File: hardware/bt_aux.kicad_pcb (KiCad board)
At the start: 2 copper layers, 51.8 x 29 mm, 18 parts, among them J1 esp32_1, J2 esp32_2, J3 audio_out, U1 PCM5102A

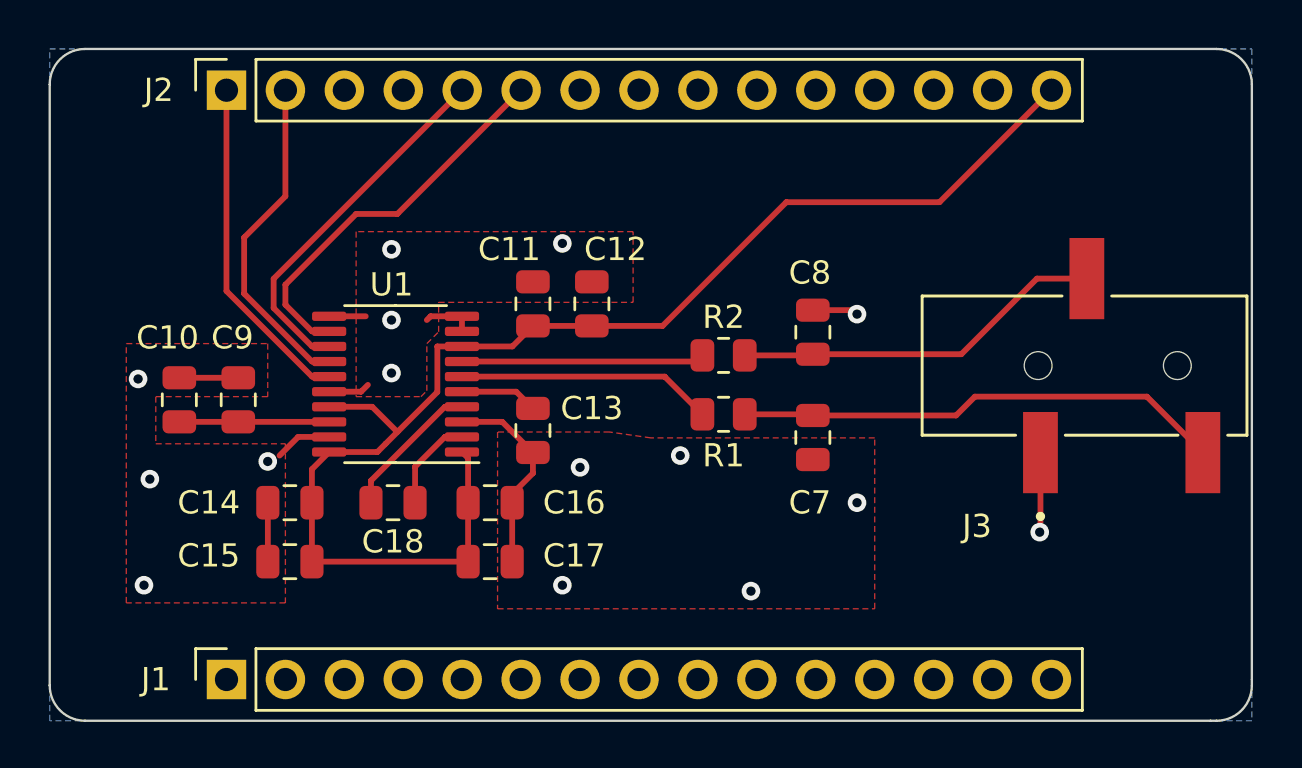
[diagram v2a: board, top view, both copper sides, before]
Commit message: fix oreintation of jack
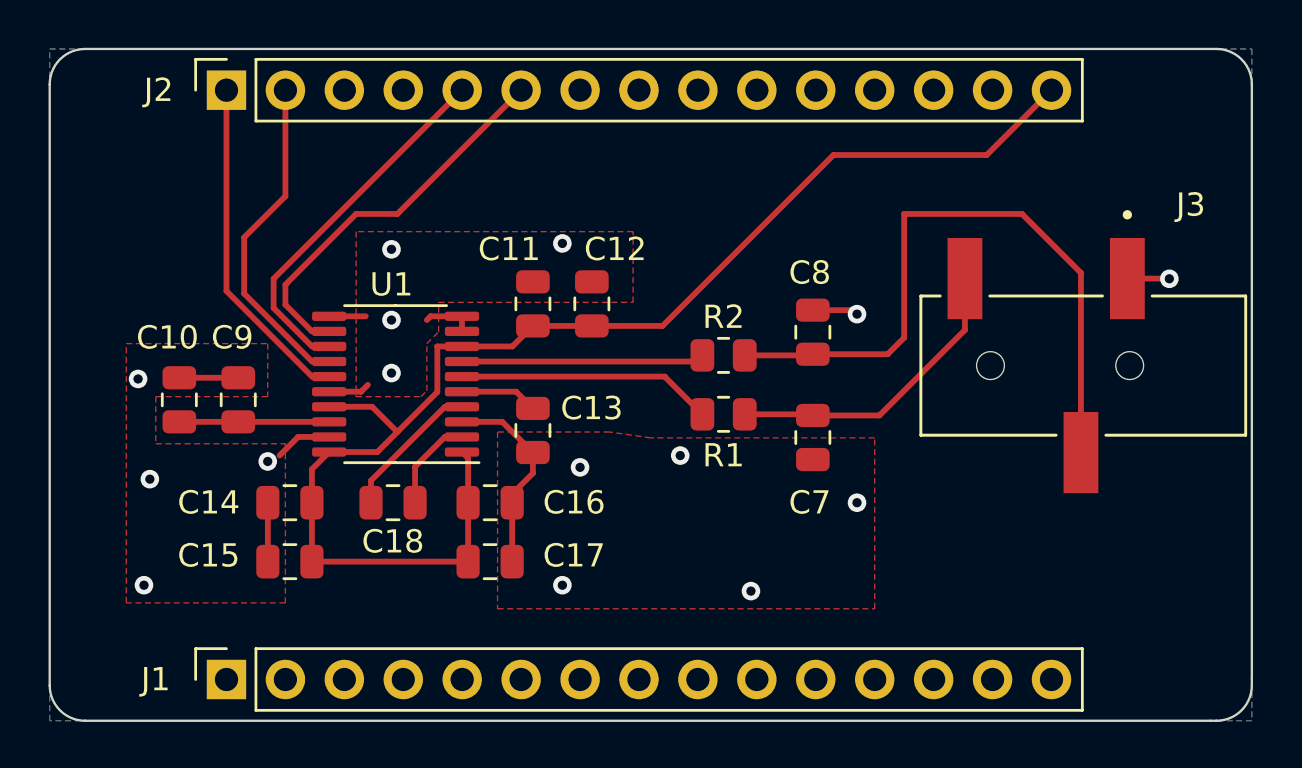
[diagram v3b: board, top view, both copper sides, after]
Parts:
- moved J3 2.05 mm to (163.7, 103.3), turned to 180 degrees
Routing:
- net /right: track 16.1 -> 28.9 mm
- net /left: track 21.1 -> 13.3 mm
- net GND: track 27.5 -> 25.6 mm
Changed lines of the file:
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@@
   )
   (footprint "audio-jack:BOOMELE_PJ-320B" (layer "F.Cu")
-    (at 165.746 103.31)
+    (at 163.692 103.31 180)
     (property "Link" "https://jlcpcb.com/partdetail/boomele_boom_Precision_elec-C18594/C18594")
     (property "Sheetfile" "bt_aux.kicad_sch")
@@
     (fp_circle (center -2.9 6.5) (end -2.8 6.5)
       (stroke (width 0.2) (type solid)) (fill none) (layer "F.Fab"))
-    (pad "" np_thru_hole circle (at -3 0) (size 1.2 1.2) (drill 1.2) (layers "*.Cu" "*.Mask"))
-    (pad "" np_thru_hole circle (at 3 0) (size 1.2 1.2) (drill 1.2) (layers "*.Cu" "*.Mask"))
-    (pad "R" smd rect (at -0.9 -3.75) (size 1.5 3.5) (layers "F.Cu" "F.Paste" "F.Mask")
+    (pad "" np_thru_hole circle (at -3 0 180) (size 1.2 1.2) (drill 1.2) (layers "*.Cu" "*.Mask"))
+    (pad "" np_thru_hole circle (at 3 0 180) (size 1.2 1.2) (drill 1.2) (layers "*.Cu" "*.Mask"))
+    (pad "R" smd rect (at -0.9 -3.75 180) (size 1.5 3.5) (layers "F.Cu" "F.Paste" "F.Mask")
       (net 3 "/right") (pintype "passive") (solder_mask_margin 0.102))
-    (pad "S" smd rect (at -2.9 3.75) (size 1.5 3.5) (layers "F.Cu" "F.Paste" "F.Mask")
+    (pad "S" smd rect (at -2.9 3.75 180) (size 1.5 3.5) (layers "F.Cu" "F.Paste" "F.Mask")
       (net 2 "GND") (pintype "passive") (solder_mask_margin 0.102))
-    (pad "T" smd rect (at 4.1 3.75) (size 1.5 3.5) (layers "F.Cu" "F.Paste" "F.Mask")
+    (pad "T" smd rect (at 4.1 3.75 180) (size 1.5 3.5) (layers "F.Cu" "F.Paste" "F.Mask")
       (net 1 "/left") (pintype "passive") (solder_mask_margin 0.102))
+    (model "/home/bradley/Downloads/User Library-PJ-320B.STEP"
+      (offset (xyz -0.9 0 0))
+      (scale (xyz 1 1 1))
+      (rotate (xyz 0 0 0))
+    )
   )
   (footprint "Resistor_SMD:R_0805_2012Metric" (layer "F.Cu")
@@
     (stroke (width 0.1) (type default)) (layer "Edge.Cuts"))
   (segment (start 152.985 105.41) (end 153.035 105.46) (width 0.25) (layer "F.Cu") (net 1))
-  (segment (start 167.434 104.648) (end 169.846 107.06) (width 0.25) (layer "F.Cu") (net 1))
   (segment (start 150.1 105.41) (end 152.985 105.41) (width 0.25) (layer "F.Cu") (net 1))
-  (segment (start 160.02 104.648) (end 167.434 104.648) (width 0.25) (layer "F.Cu") (net 1))
-  (segment (start 159.208 105.46) (end 160.02 104.648) (width 0.25) (layer "F.Cu") (net 1))
-  (segment (start 153.035 105.46) (end 159.208 105.46) (width 0.25) (layer "F.Cu") (net 1))
+  (segment (start 159.592 101.774) (end 155.906 105.46) (width 0.25) (layer "F.Cu") (net 1))
+  (segment (start 159.592 99.56) (end 159.592 101.774) (width 0.25) (layer "F.Cu") (net 1))
+  (segment (start 155.906 105.46) (end 153.035 105.46) (width 0.25) (layer "F.Cu") (net 1))
   (segment (start 139.649 105.735) (end 137.9125 105.735) (width 0.25) (layer "F.Cu") (net 2))
-  (segment (start 162.846 110.458) (end 162.814 110.49) (width 0.25) (layer "F.Cu") (net 2))
   (segment (start 140.076 108.844) (end 140.97 107.95) (width 0.25) (layer "F.Cu") (net 2))
   (segment (start 128.27 103.835) (end 125.73 103.835) (width 0.25) (layer "F.Cu") (net 2))
   (segment (start 153.035 100.92) (end 154.768 100.92) (width 0.25) (layer "F.Cu") (net 2))
-  (segment (start 162.846 107.06) (end 162.846 110.458) (width 0.25) (layer "F.Cu") (net 2))
   (segment (start 137.9125 101.185) (end 137.9125 101.835) (width 0.25) (layer "F.Cu") (net 2))
   (segment (start 140.076 109.22) (end 140.076 108.844) (width 0.25) (layer "F.Cu") (net 2))
+  (segment (start 168.394 99.56) (end 168.402 99.568) (width 0.25) (layer "F.Cu") (net 2))
   (segment (start 137.9125 101.185) (end 136.559 101.185) (width 0.25) (layer "F.Cu") (net 2))
-  (segment (start 163.01 110.294) (end 162.814 110.49) (width 0.25) (layer "F.Cu") (net 2))
   (segment (start 140.97 107.95) (end 140.97 107.056) (width 0.25) (layer "F.Cu") (net 2))
   (segment (start 132.1875 101.185) (end 133.765 101.185) (width 0.25) (layer "F.Cu") (net 2))
@@
   (segment (start 132.1875 106.385) (end 130.851 106.385) (width 0.25) (layer "F.Cu") (net 2))
   (segment (start 140.97 107.056) (end 139.649 105.735) (width 0.25) (layer "F.Cu") (net 2))
+  (segment (start 166.592 99.56) (end 168.394 99.56) (width 0.25) (layer "F.Cu") (net 2))
   (via (at 142.24 112.776) (size 0.8) (drill 0.4) (layers "F.Cu" "B.Cu") (free) (net 2))
   (via (at 124.206 112.776) (size 0.8) (drill 0.4) (layers "F.Cu" "B.Cu") (free) (net 2))
@@
   (via (at 142.24 98.044) (size 0.8) (drill 0.4) (layers "F.Cu" "B.Cu") (free) (net 2))
   (via (at 147.32 107.188) (size 0.8) (drill 0.4) (layers "F.Cu" "B.Cu") (free) (net 2))
+  (via (at 168.402 99.568) (size 0.8) (drill 0.4) (layers "F.Cu" "B.Cu") (net 2))
   (via (at 154.94 109.22) (size 0.8) (drill 0.4) (layers "F.Cu" "B.Cu") (free) (net 2))
   (via (at 150.368 113.03) (size 0.8) (drill 0.4) (layers "F.Cu" "B.Cu") (free) (net 2))
@@
   (via (at 134.874 98.298) (size 0.8) (drill 0.4) (layers "F.Cu" "B.Cu") (free) (net 2))
   (via (at 124.46 108.204) (size 0.8) (drill 0.4) (layers "F.Cu" "B.Cu") (free) (net 2))
-  (via (at 162.814 110.49) (size 0.8) (drill 0.4) (layers "F.Cu" "B.Cu") (net 2))
   (via (at 143.002 107.696) (size 0.8) (drill 0.4) (layers "F.Cu" "B.Cu") (free) (net 2))
   (via (at 134.874 103.632) (size 0.8) (drill 0.4) (layers "F.Cu" "B.Cu") (free) (net 2))
   (via (at 154.94 101.092) (size 0.8) (drill 0.4) (layers "F.Cu" "B.Cu") (net 2))
   (via (at 134.874 101.346) (size 0.8) (drill 0.4) (layers "F.Cu" "B.Cu") (free) (net 2))
-  (segment (start 162.695 99.56) (end 164.846 99.56) (width 0.25) (layer "F.Cu") (net 3))
-  (segment (start 153.035 102.82) (end 159.435 102.82) (width 0.25) (layer "F.Cu") (net 3))
+  (segment (start 156.972 102.108) (end 156.26 102.82) (width 0.25) (layer "F.Cu") (net 3))
+  (segment (start 164.592 99.314) (end 162.052 96.774) (width 0.25) (layer "F.Cu") (net 3))
+  (segment (start 156.26 102.82) (end 153.035 102.82) (width 0.25) (layer "F.Cu") (net 3))
+  (segment (start 162.052 96.774) (end 156.972 96.774) (width 0.25) (layer "F.Cu") (net 3))
   (segment (start 150.1 102.87) (end 152.985 102.87) (width 0.25) (layer "F.Cu") (net 3))
+  (segment (start 156.972 96.774) (end 156.972 102.108) (width 0.25) (layer "F.Cu") (net 3))
   (segment (start 152.985 102.87) (end 153.035 102.82) (width 0.25) (layer "F.Cu") (net 3))
-  (segment (start 159.435 102.82) (end 162.695 99.56) (width 0.25) (layer "F.Cu") (net 3))
+  (segment (start 164.592 107.06) (end 164.592 99.314) (width 0.25) (layer "F.Cu") (net 3))
   (segment (start 128.265 105.405) (end 128.27 105.41) (width 0.25) (layer "F.Cu") (net 4))
   (segment (start 128.27 105.735) (end 125.73 105.735) (width 0.25) (layer "F.Cu") (net 4))
@@
   (segment (start 134.041 105.085) (end 135.128 106.172) (width 0.25) (layer "F.Cu") (net 5))
   (segment (start 134.265 107.035) (end 132.1875 107.035) (width 0.25) (layer "F.Cu") (net 5))
-  (segment (start 158.496 96.266) (end 151.892 96.266) (width 0.25) (layer "F.Cu") (net 5))
+  (segment (start 146.558 101.6) (end 143.51 101.6) (width 0.25) (layer "F.Cu") (net 5))
   (segment (start 131.445 107.7775) (end 132.1875 107.035) (width 0.25) (layer "F.Cu") (net 5))
   (segment (start 137.9125 102.485) (end 136.85 102.485) (width 0.25) (layer "F.Cu") (net 5))
   (segment (start 136.85 104.45) (end 134.62 106.68) (width 0.25) (layer "F.Cu") (net 5))
+  (segment (start 160.528 94.234) (end 153.924 94.234) (width 0.25) (layer "F.Cu") (net 5))
   (segment (start 134.62 106.68) (end 134.265 107.035) (width 0.25) (layer "F.Cu") (net 5))
   (segment (start 131.445 111.76) (end 138.176 111.76) (width 0.25) (layer "F.Cu") (net 5))
   (segment (start 131.445 109.22) (end 131.445 107.7775) (width 0.25) (layer "F.Cu") (net 5))
-  (segment (start 151.892 96.266) (end 146.558 101.6) (width 0.25) (layer "F.Cu") (net 5))
   (segment (start 131.445 111.76) (end 131.445 109.22) (width 0.25) (layer "F.Cu") (net 5))
   (segment (start 136.85 102.485) (end 136.85 104.45) (width 0.25) (layer "F.Cu") (net 5))
   (segment (start 138.176 107.2985) (end 137.9125 107.035) (width 0.25) (layer "F.Cu") (net 5))
-  (segment (start 146.558 101.6) (end 143.51 101.6) (width 0.25) (layer "F.Cu") (net 5))
+  (segment (start 163.322 91.44) (end 160.528 94.234) (width 0.25) (layer "F.Cu") (net 5))
   (segment (start 140.97 101.6) (end 140.085 102.485) (width 0.25) (layer "F.Cu") (net 5))
-  (segment (start 163.322 91.44) (end 158.496 96.266) (width 0.25) (layer "F.Cu") (net 5))
+  (segment (start 153.924 94.234) (end 146.558 101.6) (width 0.25) (layer "F.Cu") (net 5))
   (segment (start 140.249 104.435) (end 137.9125 104.435) (width 0.25) (layer "F.Cu") (net 6))
   (segment (start 140.97 105.156) (end 140.249 104.435) (width 0.25) (layer "F.Cu") (net 6))

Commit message: modify bom, generate fab files, submit order
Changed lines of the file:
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@@
       (outputformat 1)
       (mirror false)
-      (drillshape 1)
+      (drillshape 0)
       (scaleselection 1)
-      (outputdirectory "")
+      (outputdirectory "fab/")
     )
   )
@@
     (fp_line (start 1 0.625) (end -1 0.625)
       (stroke (width 0.1) (type solid)) (layer "F.Fab"))
-    (pad "1" smd roundrect (at -0.9125 0) (size 1.025 1.4) (layers "F.Cu" "F.Paste" "F.Mask") (roundrect_rratio 0.243902)
+    (pad "1" smd roundrect (at -0.9125 0) (size 1.025 1.4) (layers "F.Cu" "F.Paste" "F.Mask") (roundrect_rratio 0.243902439)
       (net 32 "Net-(U1-OUTL)") (pintype "passive"))
-    (pad "2" smd roundrect (at 0.9125 0) (size 1.025 1.4) (layers "F.Cu" "F.Paste" "F.Mask") (roundrect_rratio 0.243902)
+    (pad "2" smd roundrect (at 0.9125 0) (size 1.025 1.4) (layers "F.Cu" "F.Paste" "F.Mask") (roundrect_rratio 0.243902439)
       (net 1 "/left") (pintype "passive"))
     (model "${KICAD6_3DMODEL_DIR}/Resistor_SMD.3dshapes/R_0805_2012Metric.wrl"
@@
     (fp_line (start 1 0.625) (end -1 0.625)
       (stroke (width 0.1) (type solid)) (layer "F.Fab"))
-    (pad "1" smd roundrect (at -0.9125 0) (size 1.025 1.4) (layers "F.Cu" "F.Paste" "F.Mask") (roundrect_rratio 0.243902)
+    (pad "1" smd roundrect (at -0.9125 0) (size 1.025 1.4) (layers "F.Cu" "F.Paste" "F.Mask") (roundrect_rratio 0.243902439)
       (net 33 "Net-(U1-OUTR)") (pintype "passive"))
-    (pad "2" smd roundrect (at 0.9125 0) (size 1.025 1.4) (layers "F.Cu" "F.Paste" "F.Mask") (roundrect_rratio 0.243902)
+    (pad "2" smd roundrect (at 0.9125 0) (size 1.025 1.4) (layers "F.Cu" "F.Paste" "F.Mask") (roundrect_rratio 0.243902439)
       (net 3 "/right") (pintype "passive"))
     (model "${KICAD6_3DMODEL_DIR}/Resistor_SMD.3dshapes/R_0805_2012Metric.wrl"
